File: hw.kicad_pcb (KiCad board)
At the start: 4 copper layers, 75 x 75 mm, 160 parts, among them IC2 ESDALC6V1W5, IC3 ESDALC6V1W5, IC4 PCMD3180IRTWT, IC5 ICM-20948, J1 RECE.20279.001E.01, J2 RECE.20279.001E.01, J3 78800-0001, J4 10164227-1004A1RLF, J5 10164227-1004A1RLF, J7 USB4105-GF-A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

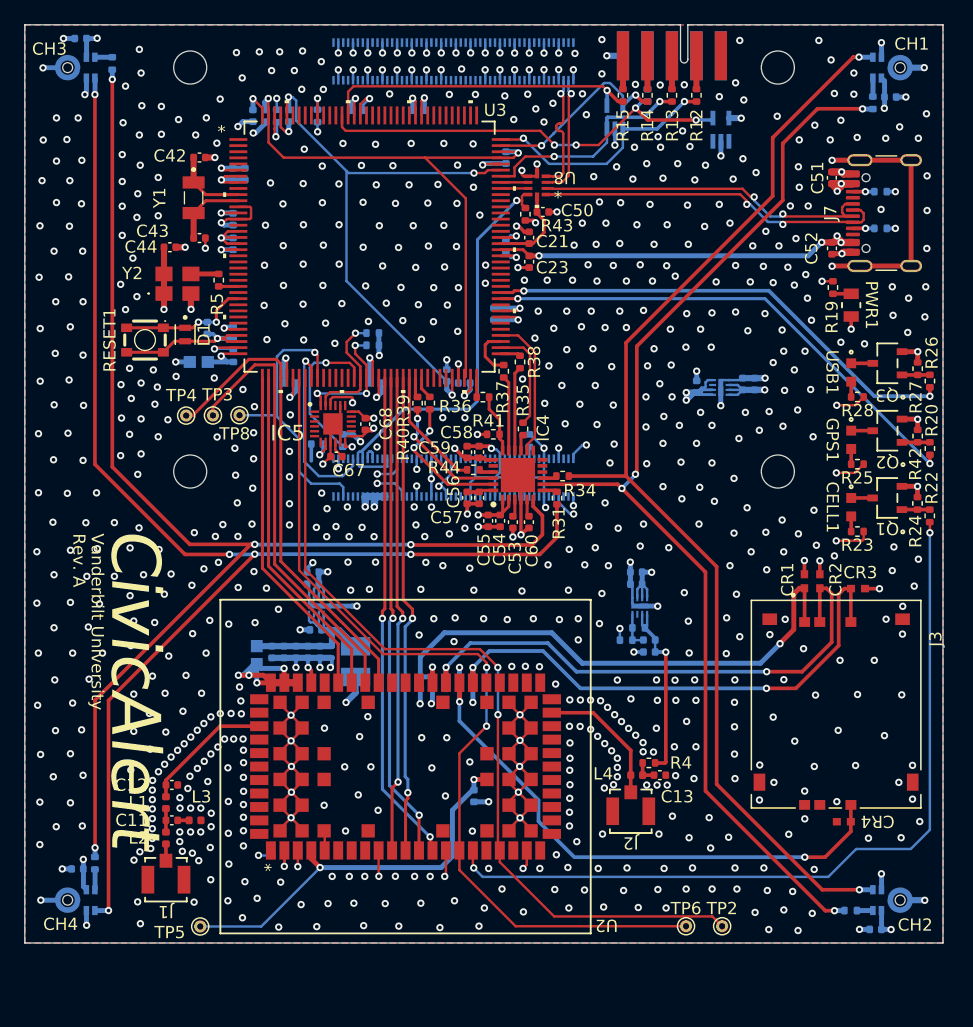
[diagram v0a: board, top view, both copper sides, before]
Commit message: Fix RF trace impedances
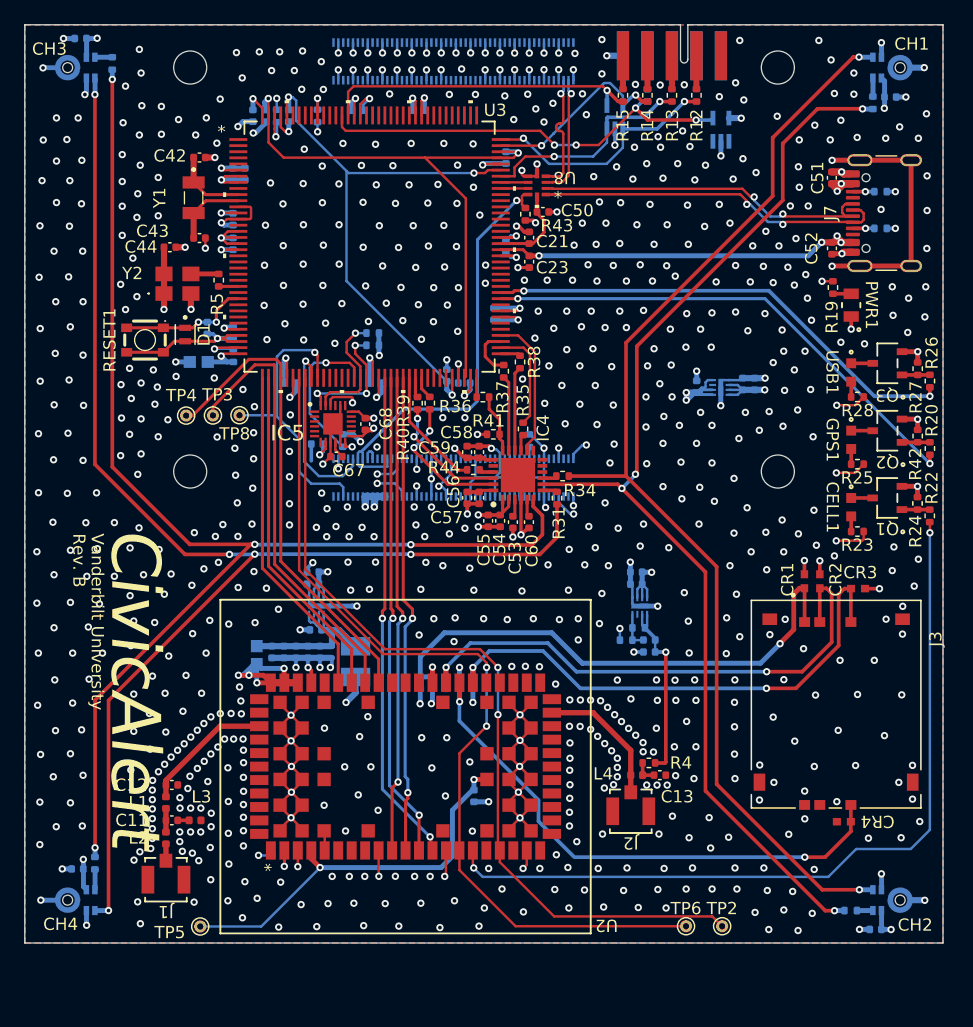
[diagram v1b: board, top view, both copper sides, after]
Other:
- board text added: "Rev. B"
- board text removed: "Rev. A"

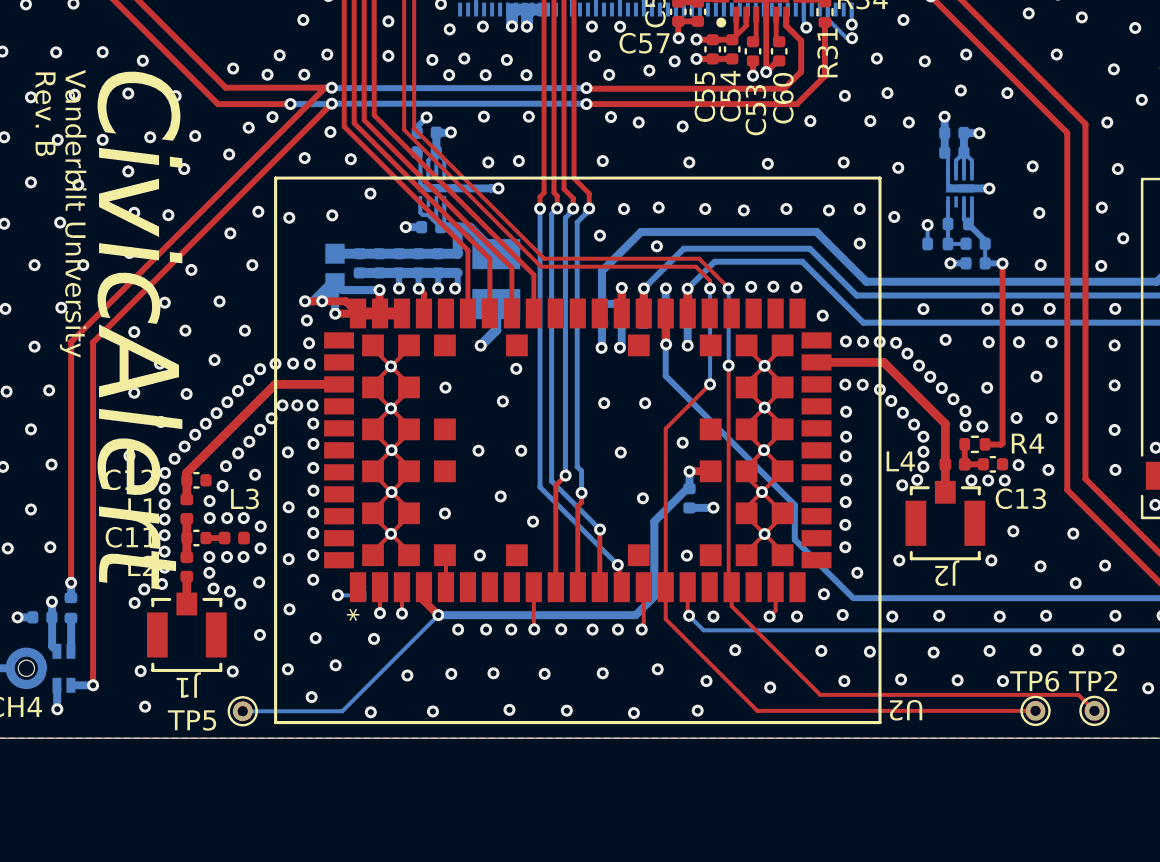
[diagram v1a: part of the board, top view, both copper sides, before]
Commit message: Update silkscreen, add modem +5V via to regulator
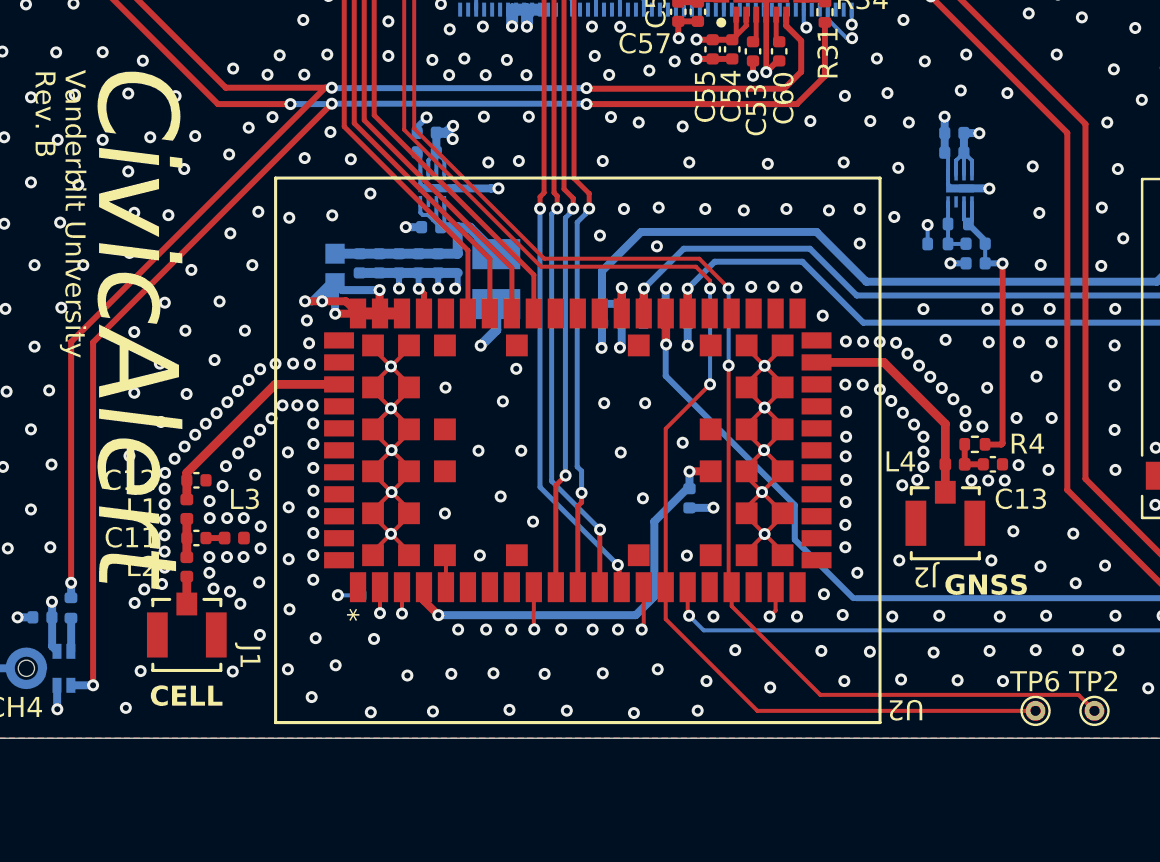
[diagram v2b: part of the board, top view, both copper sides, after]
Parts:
- removed TP5: GPS_VINT, TestPoint:TestPoint_THTPad_D1.0mm_Drill0.5mm
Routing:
- net GPS_VINT: track 32.8 -> 21.0 mm
- net VCC_5V: track 64.8 -> 66.0 mm, vias 16 -> 17
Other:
- board text added: "CELL"
- board text added: "GNSS"
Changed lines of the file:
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@@
 		(tags "RECE.20279.001E.01 ")
 		(property "Reference" "J2"
-			(at 0 -2.59 180)
+			(at 0.9956 -2.67 180)
 			(unlocked yes)
 			(layer "F.SilkS")
@@
 		(embedded_fonts no)
 	)
-	(footprint "TestPoint:TestPoint_THTPad_D1.0mm_Drill0.5mm"
-		(layer "F.Cu")
-		(at 115.4006 138.89)
-		(descr "THT pad as test Point, diameter 1.0mm, hole diameter 0.5mm")
-		(tags "test point THT pad")
-		(property "Reference" "TP5"
-			(at -2.48 0.49 0)
-			(layer "F.SilkS")
-			(effects
-				(font
-					(size 1 1)
-					(thickness 0.15)
-				)
-			)
-		)
-		(property "Value" "GPS_VINT"
-			(at 0 1.55 0)
-			(layer "F.Fab")
-			(effects
-				(font
-					(size 1 1)
-					(thickness 0.15)
-				)
-			)
-		)
-		(property "Datasheet" ""
-			(at 0 0 0)
-			(unlocked yes)
-			(layer "F.Fab")
-			(hide yes)
-			(effects
-				(font
-					(size 1.27 1.27)
-					(thickness 0.15)
-				)
-			)
-		)
-		(property "Description" "test point"
-			(at 0 0 0)
-			(unlocked yes)
-			(layer "F.Fab")
-			(hide yes)
-			(effects
-				(font
-					(size 1.27 1.27)
-					(thickness 0.15)
-				)
-			)
-		)
-		(property "MPN" ""
-			(at 0 0 0)
-			(unlocked yes)
-			(layer "F.Fab")
-			(hide yes)
-			(effects
-				(font
-					(size 1 1)
-					(thickness 0.15)
-				)
-			)
-		)
-		(property ki_fp_filters "Pin* Test*")
-		(sheetname "/GPS + Cellular/")
-		(sheetfile "gps_cellular.kicad_sch")
-		(attr exclude_from_pos_files exclude_from_bom)
-		(fp_circle
-			(center 0 0)
-			(end 0 0.7)
-			(stroke
-				(width 0.12)
-				(type solid)
-			)
-			(fill no)
-			(layer "F.SilkS")
-		)
-		(fp_circle
-			(center 0 0)
-			(end 1 0)
-			(stroke
-				(width 0.05)
-				(type solid)
-			)
-			(fill no)
-			(layer "F.CrtYd")
-		)
-		(fp_text user "${REFERENCE}"
-			(at 0 -1.45 0)
-			(layer "F.Fab")
-			(effects
-				(font
-					(size 1 1)
-					(thickness 0.15)
-				)
-			)
-		)
-		(pad "1" thru_hole circle
-			(at 0 0)
-			(size 1 1)
-			(drill 0.5)
-			(layers "*.Cu" "*.Mask")
-			(remove_unused_layers no)
-			(net 195 "GPS_VINT")
-			(pinfunction "1")
-			(pintype "passive")
-		)
-		(embedded_fonts no)
-	)
 	(footprint "Capacitor_SMD:C_0402_1005Metric"
 		(layer "F.Cu")
@@
 		(tags "RECE.20279.001E.01 ")
 		(property "Reference" "J1"
-			(at 0 -2.61 180)
+			(at -3.1494 -1.09 270)
 			(unlocked yes)
 			(layer "F.SilkS")
@@
 		)
 	)
+	(gr_text "CELL"
+		(at 110.73 138.73 0)
+		(layer "F.SilkS")
+		(effects
+			(font
+				(size 1 1)
+				(thickness 0.2)
+				(bold yes)
+			)
+			(justify left bottom)
+		)
+	)
 	(gr_text "Rev. B"
 		(at 104.91 106.78 270)
@@
 		)
 	)
+	(gr_text "GNSS"
+		(at 150.5 133.17 0)
+		(layer "F.SilkS")
+		(effects
+			(font
+				(size 1 1)
+				(thickness 0.2)
+				(bold yes)
+			)
+			(justify left bottom)
+		)
+	)
 	(gr_text "{\n  \"ViaStitching\": \"0.2\",\n  \"GND_PLANE\": {\n    \"HSpacing\": \"2\",\n    \"VSpacing\": \"2\",\n    \"Clearance\": \"0\",\n    \"Randomize\": true\n  }\n}"
 		(at 0 0 0)
@@
 	)
 	(via
-		(at 110.513878 138.661191)
+		(at 109.55 138.72)
 		(size 0.6)
 		(drill 0.3)
@@
 	)
 	(segment
-		(start 120.38 138.89)
-		(end 125.19 134.08)
-		(width 0.2)
-		(layer "B.Cu")
-		(net 195)
-	)
-	(segment
-		(start 115.4006 138.89)
-		(end 120.38 138.89)
-		(width 0.2)
-		(layer "B.Cu")
-		(net 195)
-	)
-	(segment
 		(start 135.07 134.08)
 		(end 136 133.15)
@@
 	)
 	(via
+		(at 125.91 110.25)
+		(size 0.6)
+		(drill 0.3)
+		(layers "F.Cu" "B.Cu")
+		(net 202)
+	)
+	(via
 		(at 128.88 104.61)
 		(size 0.6)
@@
 	)
 	(via
-		(at 125.819999 109.9161)
+		(at 125.93 109.59)
 		(size 0.6)
 		(drill 0.3)
@@
 	)
 	(segment
-		(start 125.089999 109.9361)
-		(end 125.799999 109.9361)
-		(width 0.4)
-		(layer "B.Cu")
-		(net 202)
-	)
-	(segment
 		(start 159.7063 95.06)
 		(end 160.6863 95.06)
@@
 	)
 	(segment
+		(start 125.089999 109.9361)
+		(end 125.5839 109.9361)
+		(width 0.5)
+		(layer "B.Cu")
+		(net 202)
+	)
+	(segment
+		(start 125.5961 109.9361)
+		(end 125.91 110.25)
+		(width 0.4)
+		(layer "B.Cu")
+		(net 202)
+	)
+	(segment
 		(start 158.5806 72.86)
 		(end 159.58 72.86)
@@
 	)
 	(segment
+		(start 125.5839 109.9361)
+		(end 125.93 109.59)
+		(width 0.5)
+		(layer "B.Cu")
+		(net 202)
+	)
+	(segment
 		(start 128.8816 103.7784)
 		(end 128.8816 104.6084)
@@
 	)
 	(segment
+		(start 125.089999 109.9361)
+		(end 125.5961 109.9361)
+		(width 0.4)
+		(layer "B.Cu")
+		(net 202)
+	)
+	(segment
 		(start 158.5931 95.459999)
 		(end 159.306301 95.459999)
@@
 	)
 	(segment
-		(start 125.799999 109.9361)
-		(end 125.819999 109.9161)
-		(width 0.4)
-		(layer "B.Cu")
-		(net 202)
-	)
-	(segment
 		(start 130.3002 103.7896)
 		(end 130.46 103.7896)
@@
 	)
 	(zone
-		(net 4)
-		(net_name "Net-(U2-ANT)")
+		(net 10)
+		(net_name "Net-(J2-SIGNAL)")
 		(layer "F.Cu")
 		(name "$teardrop_padvia$")
 		(hatch full 0.1)
-		(priority 30002)
+		(priority 30000)
 		(attr
 			(teardrop
@@
 		(polygon
 			(pts
-				(xy 119.064901 122.309999) (xy 119.064901 122.749999) (xy 119.471301 122.936399) (xy 120.221601 122.529999)
-				(xy 119.471301 122.123599)
+				(xy 150.7856 126.837801) (xy 150.3456 126.837801) (xy 150.0449 127.358501) (xy 150.5656 127.931001)
+				(xy 151.0863 127.358501)
 			)
 		)
 	)
 	(zone
-		(net 10)
-		(net_name "Net-(J2-SIGNAL)")
+		(net 232)
+		(net_name "Net-(J1-SIGNAL)")
 		(layer "F.Cu")
 		(name "$teardrop_padvia$")
 		(hatch full 0.1)
-		(priority 30003)
+		(priority 30001)
 		(attr
 			(teardrop
@@
 		(polygon
 			(pts
-				(xy 145.276299 121.649999) (xy 145.276299 121.209999) (xy 144.869899 121.023599) (xy 144.119599 121.429999)
-				(xy 144.869899 121.836399)
+				(xy 112.8206 132.427801) (xy 112.3806 132.427801) (xy 112.0799 132.948501) (xy 112.6006 133.521001)
+				(xy 113.1213 132.948501)
 			)
 		)
 	)
 	(zone
-		(net 232)
-		(net_name "Net-(J1-SIGNAL)")
+		(net 4)
+		(net_name "Net-(U2-ANT)")
 		(layer "F.Cu")
 		(name "$teardrop_padvia$")
 		(hatch full 0.1)
-		(priority 30001)
+		(priority 30002)
 		(attr
 			(teardrop
@@
 		(polygon
 			(pts
-				(xy 112.8206 132.427801) (xy 112.3806 132.427801) (xy 112.0799 132.948501) (xy 112.6006 133.521001)
-				(xy 113.1213 132.948501)
+				(xy 119.064901 122.309999) (xy 119.064901 122.749999) (xy 119.471301 122.936399) (xy 120.221601 122.529999)
+				(xy 119.471301 122.123599)
+			)
+		)
+	)
+	(zone
+		(net 10)
+		(net_name "Net-(J2-SIGNAL)")
+		(layer "F.Cu")
+		(name "$teardrop_padvia$")
+		(hatch full 0.1)
+		(priority 30003)
+		(attr
+			(teardrop
+				(type padvia)
+			)
+		)
+		(connect_pads yes
+			(clearance 0)
+		)
+		(min_thickness 0.0254)
+		(filled_areas_thickness no)
+		(fill yes
+			(thermal_gap 0.5)
+			(thermal_bridge_width 0.5)
+			(island_removal_mode 1)
+			(island_area_min 10)
+		)
+		(polygon
+			(pts
+				(xy 145.276299 121.649999) (xy 145.276299 121.209999) (xy 144.869899 121.023599) (xy 144.119599 121.429999)
+				(xy 144.869899 121.836399)
 			)
 		)
@@
 			)
 		)
-	)
-	(zone
-		(net 10)
-		(net_name "Net-(J2-SIGNAL)")
-		(layer "F.Cu")
-		(name "$teardrop_padvia$")
-		(hatch full 0.1)
-		(priority 30000)
-		(attr
-			(teardrop
-				(type padvia)
-			)
-		)
-		(connect_pads yes
-			(clearance 0)
-		)
-		(min_thickness 0.0254)
-		(filled_areas_thickness no)
-		(fill yes
-			(thermal_gap 0.5)
-			(thermal_bridge_width 0.5)
-			(island_removal_mode 1)
-			(island_area_min 10)
-		)
-		(polygon
-			(pts
-				(xy 150.7856 126.837801) (xy 150.3456 126.837801) (xy 150.0449 127.358501) (xy 150.5656 127.931001)
-				(xy 151.0863 127.358501)
-			)
-		)

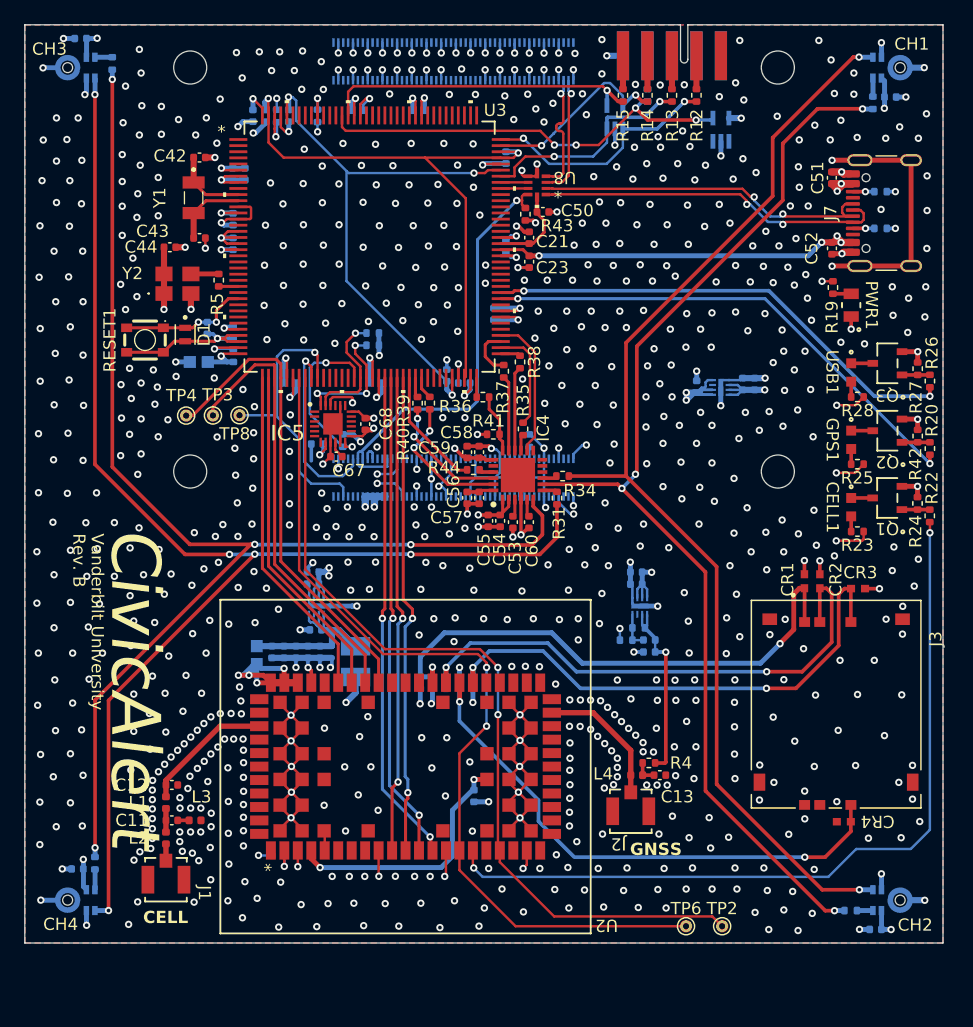
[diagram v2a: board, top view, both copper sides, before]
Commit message: New structure for holding parts, symbols, and footprints
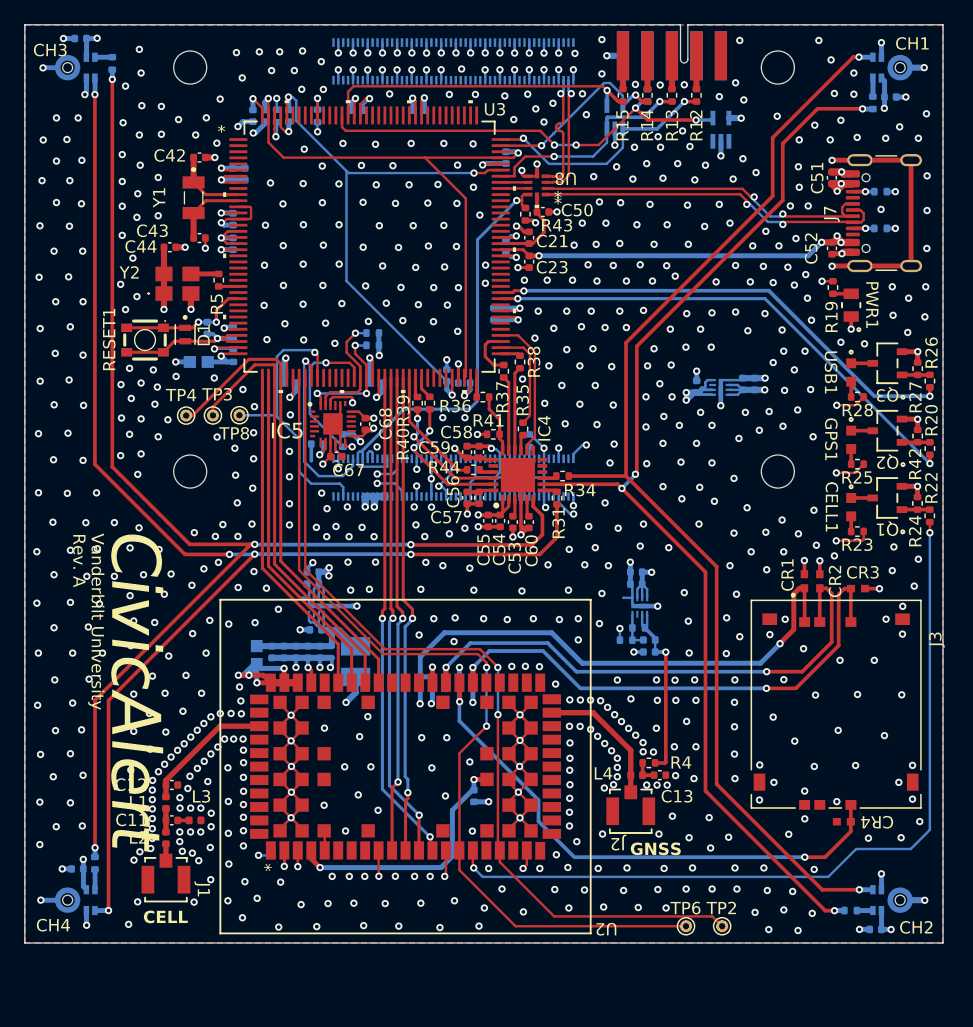
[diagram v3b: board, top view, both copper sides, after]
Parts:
- B1: footprint 009159010061911:009159010061911 -> CivicAlert:009159010061911
- C69: footprint T520B337M006ATE040:CAPMP3.7X2.8_2N_KEM -> CivicAlert:T520B337M006ATE040
- CELL1, GPS1, USB1: footprint LTST-C193TBKT-5A:LED_LTST-C_LTO -> CivicAlert:LTST-C193TBKT-5A
- CH1, CH2, CH3, CH4: footprint IM73D122V01XTMA1:PG-LLGA-5-2_INF -> CivicAlert:IM73D122V01XTMA1
- CR1, CR2, CR3, CR4: footprint PESD0402-140:PESD0402-140_LTF -> CivicAlert:PESD0402-140_LTF
- D1: footprint NSPM2051MUT5G:DIODFN160X100X55-2N -> CivicAlert:NSPM2051MUT5G
- FL1: footprint BLM18EG221SN1D:BEADC1608X95N -> CivicAlert:BLM18EG221SN1D
- FL2: footprint BLM18EG221SN1D:BEADC1608X95N -> CivicAlert:FCM1608KF-601T03
- IC2, IC3: footprint ESDALC6V1W5:SOT65P210X110-5N -> CivicAlert:ESDALC6V1W5
- IC4: value PCMD3180IRTWT -> QFN50P400X400X80-25N-D; footprint PCMD3180IRTWR:QFN50P400X400X80-25N-D -> CivicAlert:PCMD3180IRTWT
- IC5: value ICM-20948 -> QFN40P300X300X105-25N-D; footprint ICM-20948:QFN40P300X300X105-25N-D -> CivicAlert:ICM-20948
- J1, J2: footprint RECE.20279.001E.01:CON3_RECE.20279.001E.01_TAL -> CivicAlert:RECE.20279.001E.01
- J3: footprint 0788000001:MOLEX_0788000001 -> CivicAlert:0788000001
- J4, J5: value 10164227-1004A1RLF -> AMPHENOL_10164227-1004A1RLF; footprint 10164227-1004A1RLF:AMPHENOL_10164227-1004A1RLF_NOPINS -> CivicAlert:10164227-1004A1RLF
- Module1: footprint RPI-CM5:Raspberry-Pi-5-Compute-Module -> CivicAlert:RPI-CM5IO
- PWR1: footprint LTST-C170KRKT:LED_LTST-C170KRKT_LTO -> CivicAlert:LTST-C170KRKT
- Q1, Q2, Q3: footprint BC847CE6327HTSA1:PG-SOT23-3-1_INF -> CivicAlert:BC847CE6327HTSA1
- RESET1: footprint LS38G2F-T:SW-SMD_4P-L3.3-W3.1_LS38G2-T -> CivicAlert:LS38G2F-T
- U11, U5: value NCP186BMX185TAG -> XDFN8_1P7X1P3_ONS; footprint NCP186BMX185TAG:XDFN8_1P7X1P3_ONS -> CivicAlert:NCP186BMX185TAG
- U2: value LENA-R8001M10-00C -> MOD100_LENA-R8_UBL; footprint LENA-R8001M10-00C:MOD100_LENA-R8_UBL -> CivicAlert:LENA-R8001M10-00C
- U3: footprint STM32H745ZIT6:LQFP-144 -> CivicAlert:STM32H745ZIT6
- U4: value NCP186AMX390TAG -> XDFN8_1P7X1P3_ONS; footprint NCP186AMX390TAG:XDFN8_1P7X1P3_ONS -> CivicAlert:NCP186AMX390TAG
- U8: footprint TS3USB221RSER:TS3USB221RSER -> CivicAlert:TS3USB221RSER
- Y1: footprint NX3215SA-32.768K:NX3215SA32768KEXS00AMU00003 -> CivicAlert:NX3215SA-32_768K-EXS00A-MU0000
- Y2: footprint ATX-H11-F-25.000MHZ-F25-T:ATXH11F25000MHzF25T -> CivicAlert:ATX-H11-F-25_000MHz-F25-T
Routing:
- net GND: track 308.4 -> 310.5 mm
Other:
- board text added: "Rev. A"
- board text removed: "Rev. B"
